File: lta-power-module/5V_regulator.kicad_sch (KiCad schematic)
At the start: 12 parts

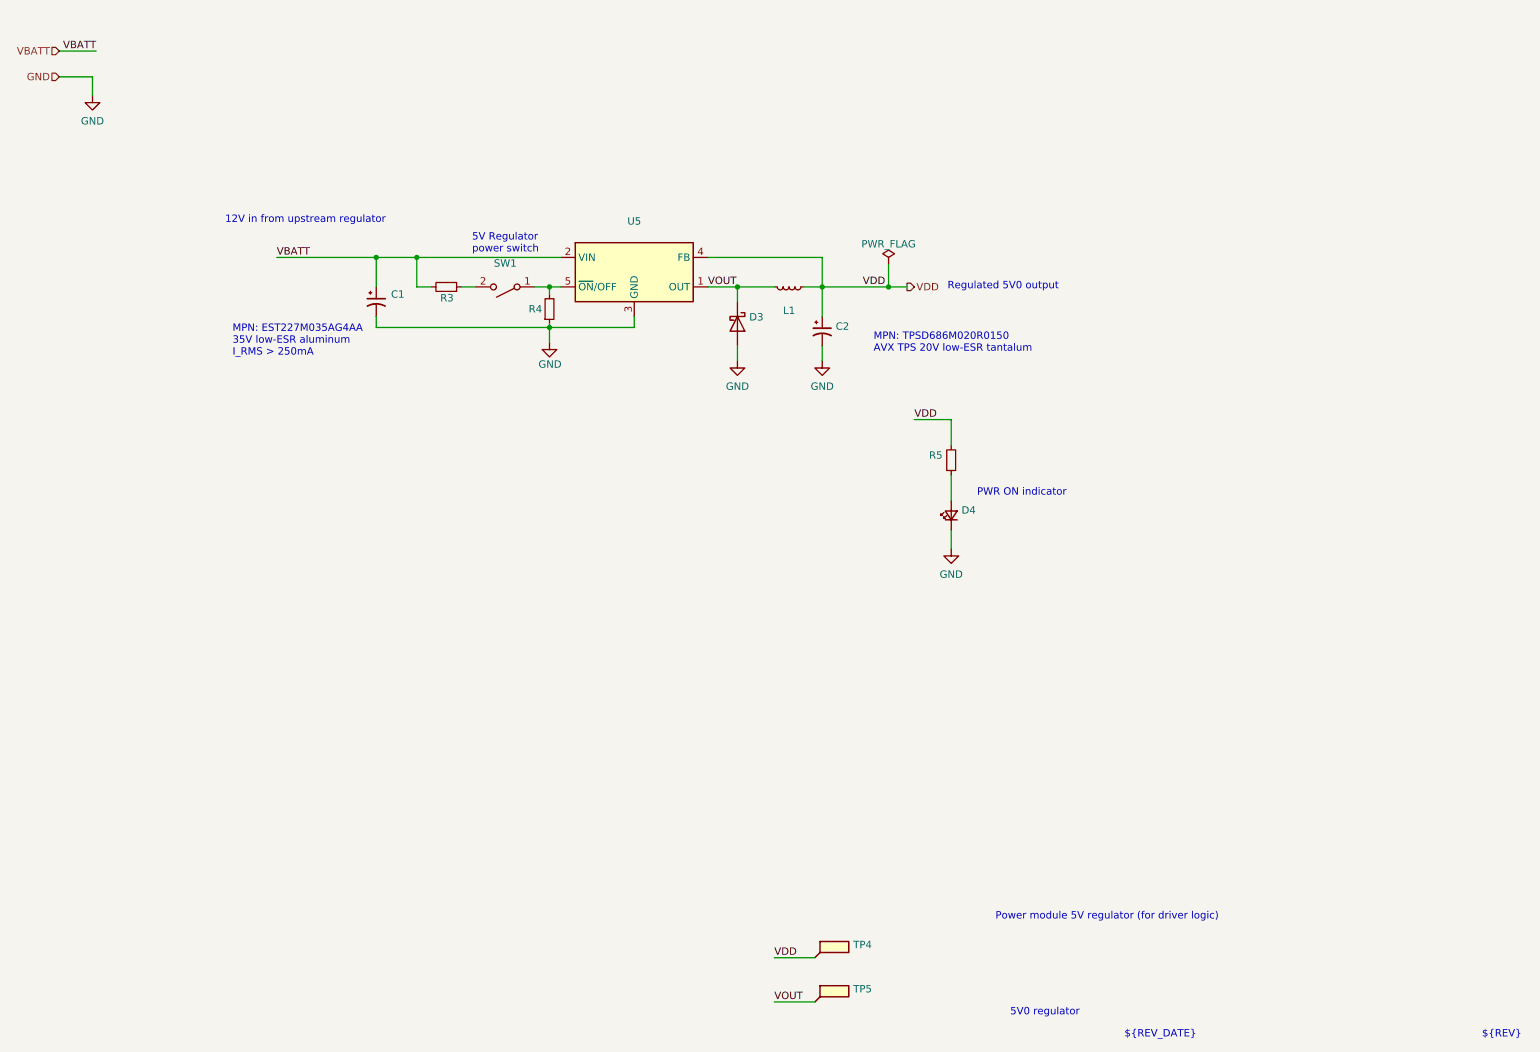
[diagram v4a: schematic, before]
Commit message: Update module footprints to be more accurate.
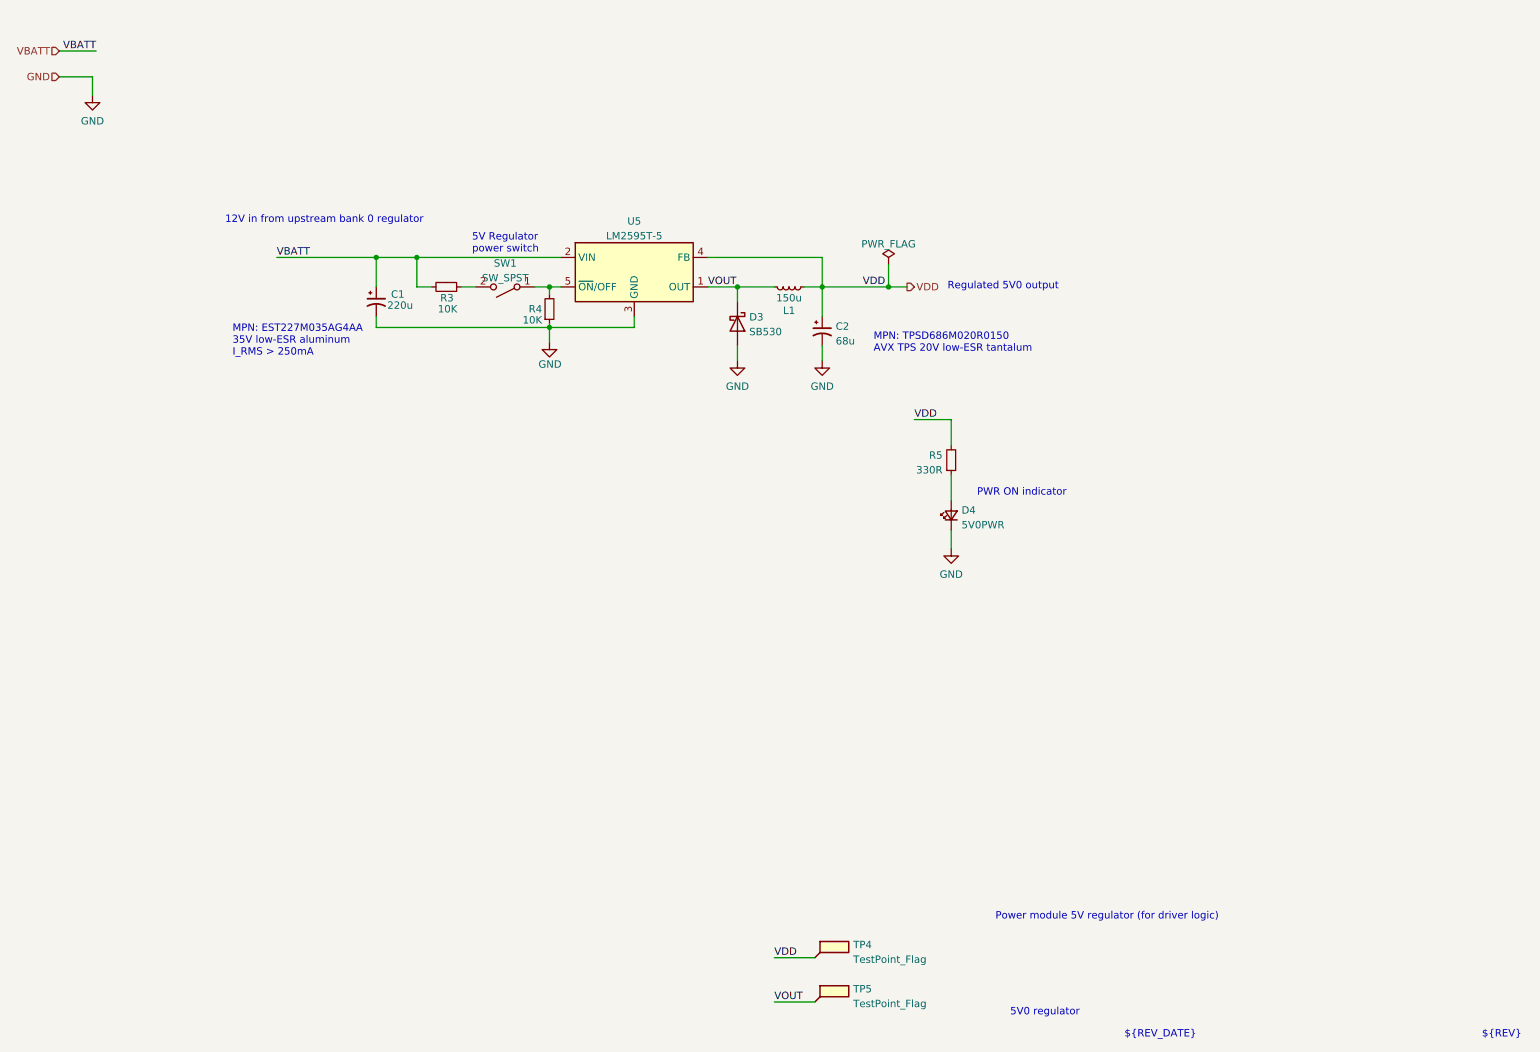
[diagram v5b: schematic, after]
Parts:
- C1: value (none) -> 220u; footprint (none) -> Capacitor_THT:CP_Radial_D8.0mm_P3.50mm
- C2: value (none) -> 68u; footprint (none) -> Capacitor_Tantalum_SMD:CP_EIA-7343-30_AVX-N_Pad2.25x2.55mm_HandSolder
- D3: value (none) -> SB530; footprint (none) -> Diode_THT:D_DO-201AD_P15.24mm_Horizontal
- D4: value (none) -> 5V0PWR; footprint (none) -> Aaron_THT:LED_D5.0mm_SilkFix
- L1: value (none) -> 150u; footprint (none) -> Aaron_THT:L_Radial_D13.5mm_P7.50mm
- R3, R4: value (none) -> 10K; footprint (none) -> Resistor_THT:R_Axial_DIN0204_L3.6mm_D1.6mm_P5.08mm_Horizontal
- R5: value (none) -> 330R; footprint (none) -> Resistor_THT:R_Axial_DIN0204_L3.6mm_D1.6mm_P5.08mm_Horizontal
- SW1: value (none) -> SW_SPST; footprint (none) -> Aaron_THT:CUI-DIP-SW_DS01-254-x-01xx
- TP4, TP5: value (none) -> TestPoint_Flag; footprint (none) -> Aaron_THT:TestPoint_THTPad_1.0x1.0mm_Drill0.3mm
- U5: value (none) -> LM2595T-5; footprint (none) -> Aaron_THT:TO-220-5_P3.4x3.7mm_StaggerOdd_Lead3.8mm_Vertical-SilkFix
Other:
- note added: "12V in from upstream bank 0 regulator"
- note removed: "12V in from upstream regulator"
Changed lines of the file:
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@@
     (effects (font (size 1.27 1.27)) (justify left bottom))
   )
-  (text "12V in from upstream regulator" (at 52.07 53.975 0)
+  (text "12V in from upstream bank 0 regulator" (at 52.07 53.975 0)
     (effects (font (size 1.27 1.27)) (justify left bottom))
   )
@@
     (in_bom yes) (on_board yes) (fields_autoplaced)
     (property "Reference" "SW1" (id 0) (at 100.33 60.6892 0))
-    (property "Value" "" (id 1) (at 100.33 63.2261 0))
-    (property "Footprint" "" (id 2) (at 100.33 64.77 0)
+    (property "Value" "SW_SPST" (id 1) (at 100.33 63.2261 0))
+    (property "Footprint" "Aaron_THT:CUI-DIP-SW_DS01-254-x-01xx" (id 2) (at 100.33 64.77 0)
       (effects (font (size 1.27 1.27)) hide)
     )
@@
       (effects (font (size 1.27 1.27)) (justify left))
     )
-    (property "Value" "" (id 1) (at 80.01 67.945 0)
-      (effects (font (size 1.27 1.27)) (justify left))
-    )
-    (property "Footprint" "" (id 2) (at 78.105 67.31 0)
+    (property "Value" "220u" (id 1) (at 80.01 67.945 0)
+      (effects (font (size 1.27 1.27)) (justify left))
+    )
+    (property "Footprint" "Capacitor_THT:CP_Radial_D8.0mm_P3.50mm" (id 2) (at 78.105 67.31 0)
       (effects (font (size 1.27 1.27)) hide)
     )
@@
       (effects (font (size 1.27 1.27)) (justify left))
     )
-    (property "Value" "" (id 1) (at 157.2641 74.0985 0)
-      (effects (font (size 1.27 1.27)) (justify left))
-    )
-    (property "Footprint" "" (id 2) (at 154.94 72.39 0)
+    (property "Value" "68u" (id 1) (at 157.2641 74.0985 0)
+      (effects (font (size 1.27 1.27)) (justify left))
+    )
+    (property "Footprint" "Capacitor_Tantalum_SMD:CP_EIA-7343-30_AVX-N_Pad2.25x2.55mm_HandSolder" (id 2) (at 154.94 72.39 0)
       (effects (font (size 1.27 1.27)) hide)
     )
@@
       (effects (font (size 1.27 1.27)) (justify right))
     )
-    (property "Value" "" (id 1) (at 92.075 68.58 90)
-      (effects (font (size 1.27 1.27)) (justify right))
-    )
-    (property "Footprint" "" (id 2) (at 90.17 64.77 0)
+    (property "Value" "10K" (id 1) (at 92.075 68.58 90)
+      (effects (font (size 1.27 1.27)) (justify right))
+    )
+    (property "Footprint" "Resistor_THT:R_Axial_DIN0204_L3.6mm_D1.6mm_P5.08mm_Horizontal" (id 2) (at 90.17 64.77 0)
       (effects (font (size 1.27 1.27)) hide)
     )
@@
     (in_bom yes) (on_board yes) (fields_autoplaced)
     (property "Reference" "U5" (id 0) (at 122.555 53.4502 0))
-    (property "Value" "" (id 1) (at 122.555 55.9871 0))
-    (property "Footprint" "" (id 2) (at 123.825 68.58 0)
+    (property "Value" "LM2595T-5" (id 1) (at 122.555 55.9871 0))
+    (property "Footprint" "Aaron_THT:TO-220-5_P3.4x3.7mm_StaggerOdd_Lead3.8mm_Vertical-SilkFix" (id 2) (at 123.825 68.58 0)
       (effects (font (size 1.27 1.27) italic) (justify left) hide)
     )
@@
       (effects (font (size 1.27 1.27)) (justify right))
     )
-    (property "Value" "" (id 1) (at 106.68 70.485 0)
-      (effects (font (size 1.27 1.27)) (justify right))
-    )
-    (property "Footprint" "" (id 2) (at 107.95 68.58 0)
+    (property "Value" "10K" (id 1) (at 106.68 70.485 0)
+      (effects (font (size 1.27 1.27)) (justify right))
+    )
+    (property "Footprint" "Resistor_THT:R_Axial_DIN0204_L3.6mm_D1.6mm_P5.08mm_Horizontal" (id 2) (at 107.95 68.58 0)
       (effects (font (size 1.27 1.27)) hide)
     )
@@
       (effects (font (size 1.27 1.27)) (justify right))
     )
-    (property "Value" "" (id 1) (at 178.943 105.7787 90)
-      (effects (font (size 1.27 1.27)) (justify right))
-    )
-    (property "Footprint" "" (id 2) (at 177.165 104.14 90)
+    (property "Value" "5V0PWR" (id 1) (at 178.943 105.7787 90)
+      (effects (font (size 1.27 1.27)) (justify right))
+    )
+    (property "Footprint" "Aaron_THT:LED_D5.0mm_SilkFix" (id 2) (at 177.165 104.14 90)
       (effects (font (size 1.27 1.27)) hide)
     )
@@
       (effects (font (size 1.27 1.27)) (justify left))
     )
-    (property "Value" "" (id 1) (at 160.274 188.2652 0)
-      (effects (font (size 1.27 1.27)) (justify left))
-    )
-    (property "Footprint" "" (id 2) (at 158.75 187.96 0)
+    (property "Value" "TestPoint_Flag" (id 1) (at 160.274 188.2652 0)
+      (effects (font (size 1.27 1.27)) (justify left))
+    )
+    (property "Footprint" "Aaron_THT:TestPoint_THTPad_1.0x1.0mm_Drill0.3mm" (id 2) (at 158.75 187.96 0)
       (effects (font (size 1.27 1.27)) hide)
     )
@@
     (in_bom yes) (on_board yes)
     (property "Reference" "L1" (id 0) (at 149.225 68.8508 90))
-    (property "Value" "" (id 1) (at 149.225 66.675 90))
-    (property "Footprint" "" (id 2) (at 149.225 64.77 0)
+    (property "Value" "150u" (id 1) (at 149.225 66.675 90))
+    (property "Footprint" "Aaron_THT:L_Radial_D13.5mm_P7.50mm" (id 2) (at 149.225 64.77 0)
       (effects (font (size 1.27 1.27)) hide)
     )
@@
       (effects (font (size 1.27 1.27)) (justify left))
     )
-    (property "Value" "" (id 1) (at 160.274 180.6452 0)
-      (effects (font (size 1.27 1.27)) (justify left))
-    )
-    (property "Footprint" "" (id 2) (at 158.75 180.34 0)
+    (property "Value" "TestPoint_Flag" (id 1) (at 160.274 180.6452 0)
+      (effects (font (size 1.27 1.27)) (justify left))
+    )
+    (property "Footprint" "Aaron_THT:TestPoint_THTPad_1.0x1.0mm_Drill0.3mm" (id 2) (at 158.75 180.34 0)
       (effects (font (size 1.27 1.27)) hide)
     )
@@
       (effects (font (size 1.27 1.27)) (justify right))
     )
-    (property "Value" "" (id 1) (at 175.6664 96.3172 0)
-      (effects (font (size 1.27 1.27)) (justify right))
-    )
-    (property "Footprint" "" (id 2) (at 177.165 94.615 0)
+    (property "Value" "330R" (id 1) (at 175.6664 96.3172 0)
+      (effects (font (size 1.27 1.27)) (justify right))
+    )
+    (property "Footprint" "Resistor_THT:R_Axial_DIN0204_L3.6mm_D1.6mm_P5.08mm_Horizontal" (id 2) (at 177.165 94.615 0)
       (effects (font (size 1.27 1.27)) hide)
     )
@@
       (effects (font (size 1.27 1.27)) (justify left))
     )
-    (property "Value" "" (id 1) (at 142.367 72.5047 90)
-      (effects (font (size 1.27 1.27)) (justify left))
-    )
-    (property "Footprint" "" (id 2) (at 140.335 71.12 0)
-      (effects (font (size 1.27 1.27)) hide)
-    )
+    (property "Value" "SB530" (id 1) (at 142.367 72.5047 90)
+      (effects (font (size 1.27 1.27)) (justify left))
+    )
+    (property "Footprint" "Diode_THT:D_DO-201AD_P15.24mm_Horizontal" (id 2) (at 140.335 71.12 0)
+      (effects (font (size 1.27 1.27)) hide)
+    )
